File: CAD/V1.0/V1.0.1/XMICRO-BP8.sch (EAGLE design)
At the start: 119 parts, among them J1 ATX24, J2 PINHD-1X2THRU, Q1 2N5088, Q2 2N4403, Q3 2N5088, U1 7408, U2 7404, U3 7430, U4 7430, U5 TL-SCSI285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

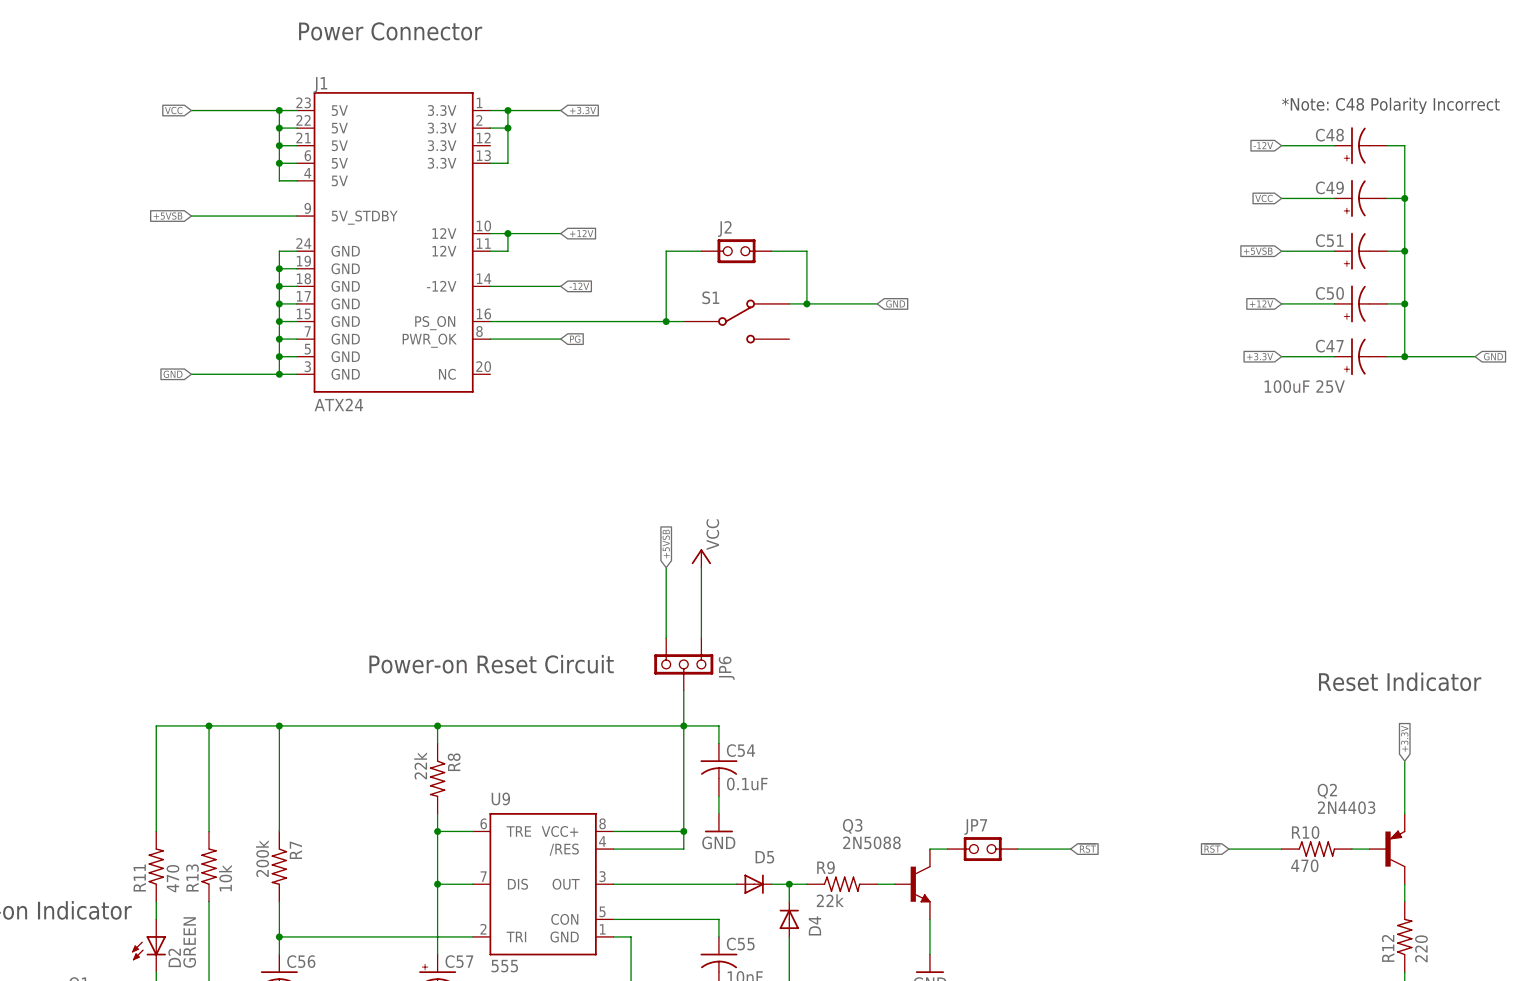
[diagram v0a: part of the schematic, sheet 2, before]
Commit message: Updated schematic xrefs to indicate signal direction.
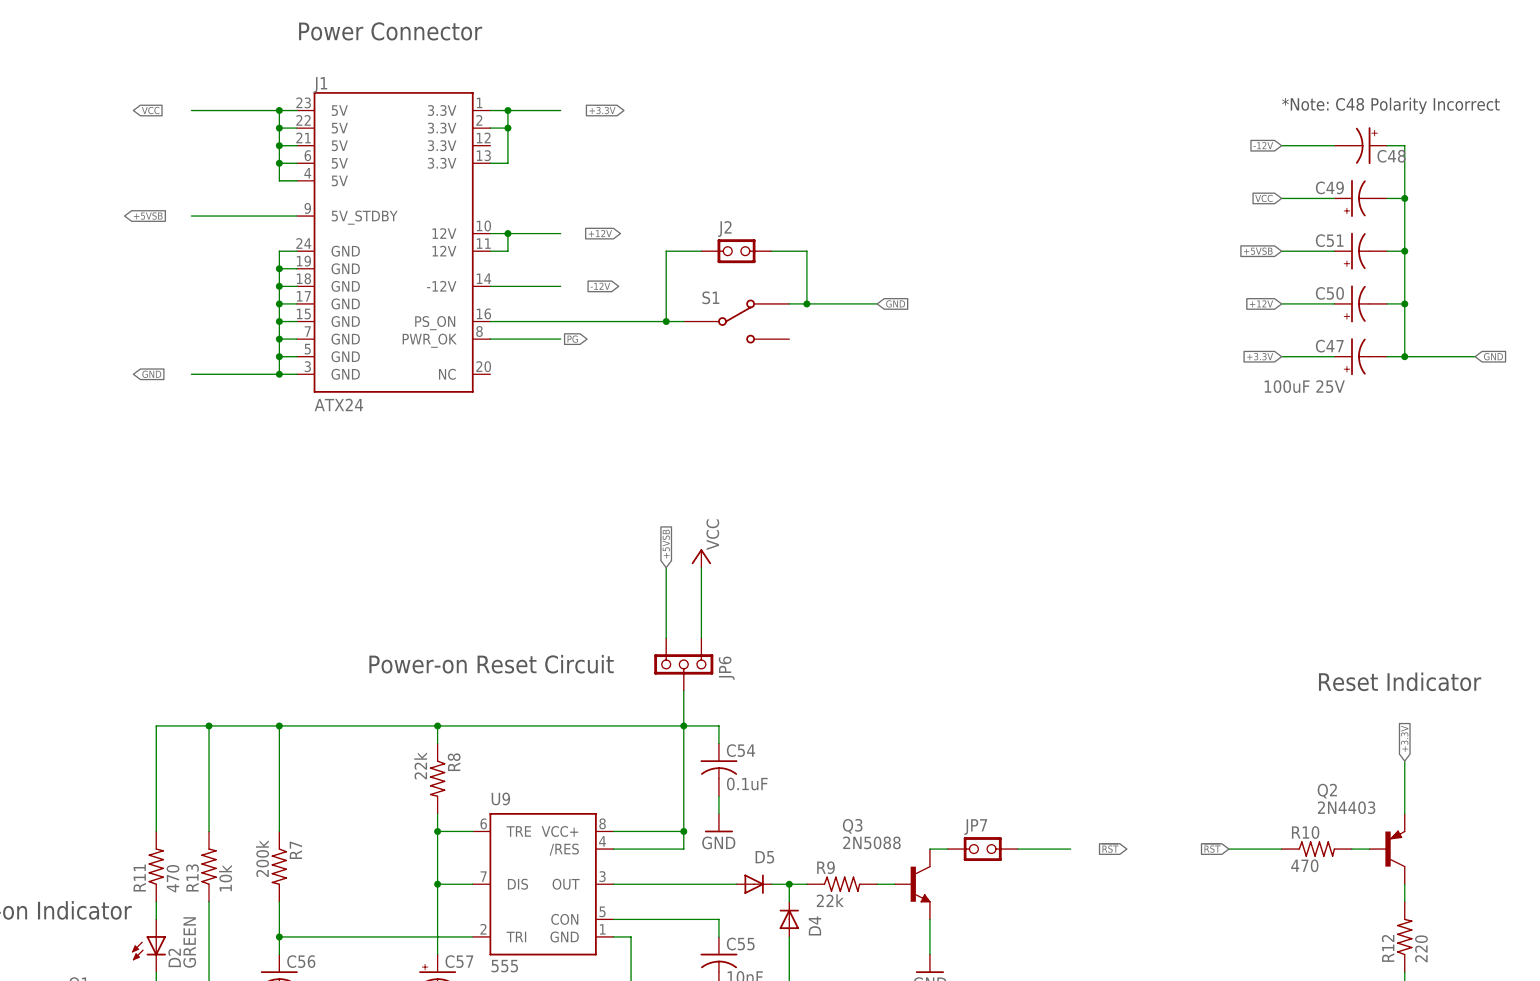
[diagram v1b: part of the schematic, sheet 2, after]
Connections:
- net -12V: now also C48.-; no longer C48.+
- net GND: now also C48.+; no longer C48.-
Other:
- moved on the sheet: C48
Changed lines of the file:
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@@
 <instance part="J1" gate="G$1" x="114.3" y="187.96"/>
 <instance part="J2" gate="G$1" x="162.56" y="185.42"/>
-<instance part="C48" gate="G$1" x="251.46" y="200.66" smashed="yes" rot="R90">
-<attribute name="NAME" x="250.444" y="201.295" size="1.778" layer="95" rot="MR0"/>
+<instance part="C48" gate="G$1" x="254" y="200.66" smashed="yes" rot="R270">
+<attribute name="NAME" x="255.016" y="200.025" size="1.778" layer="95" rot="MR180"/>
 </instance>
 <instance part="C49" gate="G$1" x="251.46" y="193.04" smashed="yes" rot="R90">
@@
 <net name="GND" class="1">
 <segment>
-<label x="83.82" y="167.64" size="1.016" layer="95" rot="R180" xref="yes"/>
 <pinref part="J1" gate="G$1" pin="GND@7"/>
 <wire x1="96.52" y1="167.64" x2="83.82" y2="167.64" width="0.1524" layer="91"/>
@@
 <junction x="96.52" y="182.88"/>
 <junction x="96.52" y="167.64"/>
-</segment>
-<segment>
-<label x="182.88" y="177.8" size="1.016" layer="95" xref="yes"/>
+<label x="75.438" y="167.64" size="1.016" layer="95" xref="yes"/>
+</segment>
+<segment>
 <wire x1="170.18" y1="177.8" x2="172.72" y2="177.8" width="0.1524" layer="91"/>
 <pinref part="J2" gate="G$1" pin="2"/>
@@
 <junction x="172.72" y="177.8"/>
 <pinref part="S1" gate="G$1" pin="P$1"/>
-</segment>
-<segment>
-<pinref part="C48" gate="G$1" pin="-"/>
+<label x="182.88" y="177.8" size="1.016" layer="95" xref="yes"/>
+</segment>
+<segment>
+<pinref part="C48" gate="G$1" pin="+"/>
 <wire x1="256.54" y1="200.66" x2="259.08" y2="200.66" width="0.1524" layer="91"/>
 <pinref part="C47" gate="G$1" pin="-"/>
@@
 <segment>
 <wire x1="129.54" y1="205.74" x2="137.16" y2="205.74" width="0.1524" layer="91"/>
-<label x="137.16" y="205.74" size="1.016" layer="95" xref="yes"/>
 <pinref part="J1" gate="G$1" pin="3.3V@0"/>
 <wire x1="127" y1="205.74" x2="129.54" y2="205.74" width="0.1524" layer="91"/>
@@
 <junction x="129.54" y="203.2"/>
 <junction x="129.54" y="205.74"/>
+<label x="146.304" y="205.74" size="1.016" layer="95" rot="R180" xref="yes"/>
 </segment>
 <segment>
@@
 <wire x1="248.92" y1="200.66" x2="241.3" y2="200.66" width="0.1524" layer="91"/>
 <label x="241.3" y="200.66" size="1.016" layer="95" rot="R180" xref="yes"/>
-<pinref part="C48" gate="G$1" pin="+"/>
-</segment>
-<segment>
-<label x="137.16" y="180.34" size="1.016" layer="95" xref="yes"/>
+<pinref part="C48" gate="G$1" pin="-"/>
+</segment>
+<segment>
 <pinref part="J1" gate="G$1" pin="-12V"/>
 <wire x1="127" y1="180.34" x2="137.16" y2="180.34" width="0.1524" layer="91"/>
+<label x="145.542" y="180.34" size="1.016" layer="95" rot="R180" xref="yes"/>
 </segment>
 </net>
@@
 <segment>
 <wire x1="127" y1="172.72" x2="137.16" y2="172.72" width="0.1524" layer="91"/>
-<label x="137.16" y="172.72" size="1.016" layer="95" rot="MR180" xref="yes"/>
 <pinref part="J1" gate="G$1" pin="PWR_OK"/>
+<label x="140.97" y="172.72" size="1.016" layer="95" rot="R180" xref="yes"/>
 </segment>
 <segment>
@@
 <segment>
 <wire x1="129.54" y1="187.96" x2="137.16" y2="187.96" width="0.1524" layer="91"/>
-<label x="137.16" y="187.96" size="1.016" layer="95" xref="yes"/>
 <pinref part="J1" gate="G$1" pin="12V@0"/>
 <wire x1="127" y1="187.96" x2="129.54" y2="187.96" width="0.1524" layer="91"/>
@@
 <wire x1="129.54" y1="185.42" x2="127" y2="185.42" width="0.1524" layer="91"/>
 <junction x="129.54" y="187.96"/>
+<label x="145.796" y="187.96" size="1.016" layer="95" rot="R180" xref="yes"/>
 </segment>
 <segment>
@@
 <segment>
 <wire x1="99.06" y1="190.5" x2="83.82" y2="190.5" width="0.1524" layer="91"/>
-<label x="83.82" y="190.5" size="1.016" layer="95" rot="R180" xref="yes"/>
 <pinref part="J1" gate="G$1" pin="5V_STDBY"/>
+<label x="74.168" y="190.5" size="1.016" layer="95" xref="yes"/>
 </segment>
 <segment>
@@
 <net name="VCC" class="0">
 <segment>
-<label x="83.82" y="205.74" size="1.016" layer="95" rot="R180" xref="yes"/>
 <pinref part="J1" gate="G$1" pin="5V@4"/>
 <wire x1="96.52" y1="205.74" x2="83.82" y2="205.74" width="0.1524" layer="91"/>
@@
 <junction x="96.52" y="203.2"/>
 <junction x="96.52" y="205.74"/>
+<label x="75.438" y="205.74" size="1.016" layer="95" xref="yes"/>
 </segment>
 <segment>
@@
 </segment>
 <segment>
-<label x="210.82" y="99.06" size="1.016" layer="95" xref="yes"/>
 <pinref part="JP7" gate="G$1" pin="2"/>
 <wire x1="203.2" y1="99.06" x2="210.82" y2="99.06" width="0.1524" layer="91"/>
+<label x="218.948" y="99.06" size="1.016" layer="95" rot="R180" xref="yes"/>
 </segment>
 </net>
@@
 <net name="!CBR" class="0">
 <segment>
-<label x="172.72" y="66.04" size="1.016" layer="95" xref="yes"/>
 <pinref part="R4" gate="G$1" pin="2"/>
 <wire x1="167.64" y1="66.04" x2="172.72" y2="66.04" width="0.1524" layer="91"/>
+<label x="181.102" y="66.04" size="1.016" layer="95" rot="R180" xref="yes"/>
 </segment>
 </net>
 <net name="!CINH" class="0">
 <segment>
-<label x="200.66" y="132.08" size="1.016" layer="95" xref="yes"/>
 <pinref part="R3" gate="G$1" pin="2"/>
 <wire x1="195.58" y1="132.08" x2="200.66" y2="132.08" width="0.1524" layer="91"/>
+<label x="209.55" y="132.08" size="1.016" layer="95" rot="R180" xref="yes"/>
 </segment>
 </net>
@@
 <segment>
 <wire x1="187.96" y1="137.16" x2="195.58" y2="137.16" width="0.1524" layer="91"/>
-<label x="195.58" y="137.16" size="1.016" layer="95" xref="yes"/>
 <pinref part="U7" gate="A" pin="Y7"/>
+<label x="203.708" y="137.16" size="1.016" layer="95" rot="R180" xref="yes"/>
 </segment>
 </net>
@@
 <segment>
 <wire x1="187.96" y1="154.94" x2="195.58" y2="154.94" width="0.1524" layer="91"/>
-<label x="195.58" y="154.94" size="1.016" layer="95" xref="yes"/>
 <pinref part="U7" gate="A" pin="Y0"/>
+<label x="203.708" y="154.94" size="1.016" layer="95" rot="R180" xref="yes"/>
 </segment>
 </net>
@@
 <segment>
 <wire x1="187.96" y1="152.4" x2="195.58" y2="152.4" width="0.1524" layer="91"/>
-<label x="195.58" y="152.4" size="1.016" layer="95" xref="yes"/>
 <pinref part="U7" gate="A" pin="Y1"/>
+<label x="203.708" y="152.4" size="1.016" layer="95" rot="R180" xref="yes"/>
 </segment>
 </net>
@@
 <segment>
 <wire x1="187.96" y1="149.86" x2="195.58" y2="149.86" width="0.1524" layer="91"/>
-<label x="195.58" y="149.86" size="1.016" layer="95" xref="yes"/>
 <pinref part="U7" gate="A" pin="Y2"/>
+<label x="203.708" y="149.86" size="1.016" layer="95" rot="R180" xref="yes"/>
 </segment>
 </net>
@@
 <segment>
 <wire x1="187.96" y1="147.32" x2="195.58" y2="147.32" width="0.1524" layer="91"/>
-<label x="195.58" y="147.32" size="1.016" layer="95" xref="yes"/>
 <pinref part="U7" gate="A" pin="Y3"/>
+<label x="203.708" y="147.32" size="1.016" layer="95" rot="R180" xref="yes"/>
 </segment>
 </net>
@@
 <segment>
 <wire x1="187.96" y1="144.78" x2="195.58" y2="144.78" width="0.1524" layer="91"/>
-<label x="195.58" y="144.78" size="1.016" layer="95" xref="yes"/>
 <pinref part="U7" gate="A" pin="Y4"/>
+<label x="203.708" y="144.78" size="1.016" layer="95" rot="R180" xref="yes"/>
 </segment>
 </net>
@@
 <segment>
 <wire x1="187.96" y1="142.24" x2="195.58" y2="142.24" width="0.1524" layer="91"/>
-<label x="195.58" y="142.24" size="1.016" layer="95" xref="yes"/>
 <pinref part="U7" gate="A" pin="Y5"/>
+<label x="203.708" y="142.24" size="1.016" layer="95" rot="R180" xref="yes"/>
 </segment>
 </net>
@@
 <segment>
 <wire x1="187.96" y1="139.7" x2="195.58" y2="139.7" width="0.1524" layer="91"/>
-<label x="195.58" y="139.7" size="1.016" layer="95" xref="yes"/>
 <pinref part="U7" gate="A" pin="Y6"/>
+<label x="203.708" y="139.7" size="1.016" layer="95" rot="R180" xref="yes"/>
 </segment>
 </net>
@@
 <wire x1="157.48" y1="121.92" x2="165.1" y2="121.92" width="0.1524" layer="91"/>
 <junction x="157.48" y="121.92"/>
-<label x="165.1" y="121.92" size="1.016" layer="95" xref="yes"/>
-</segment>
-</net>
+<label x="175.768" y="121.92" size="1.016" layer="95" rot="R180" xref="yes"/>
+</segment>
+</net>
